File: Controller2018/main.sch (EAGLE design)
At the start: 110 parts, among them Q1 MOSFET-NCHANNELDFN5X6, Q2 MOSFET-NCHANNELDFN5X6, Q3 MOSFET-NCHANNELDFN5X6, Q4 MOSFET-NCHANNELDFN5X6, Q5 MOSFET-NCHANNELDFN5X6, Q6 MOSFET-NCHANNELDFN5X6, Q7 MOSFET-PCHANNEL, U1 TEENSY_3.0+4, U2 DRV8301

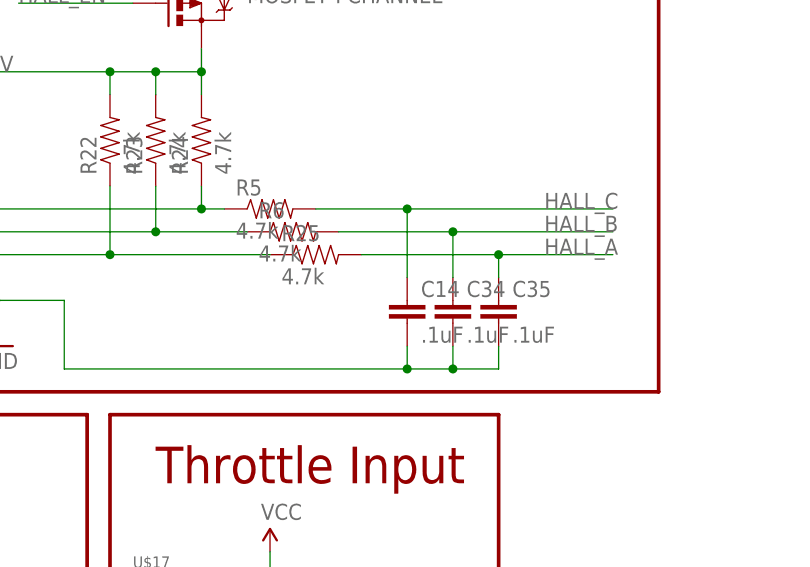
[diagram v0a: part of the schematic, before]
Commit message: Updated controller values to be more realistic
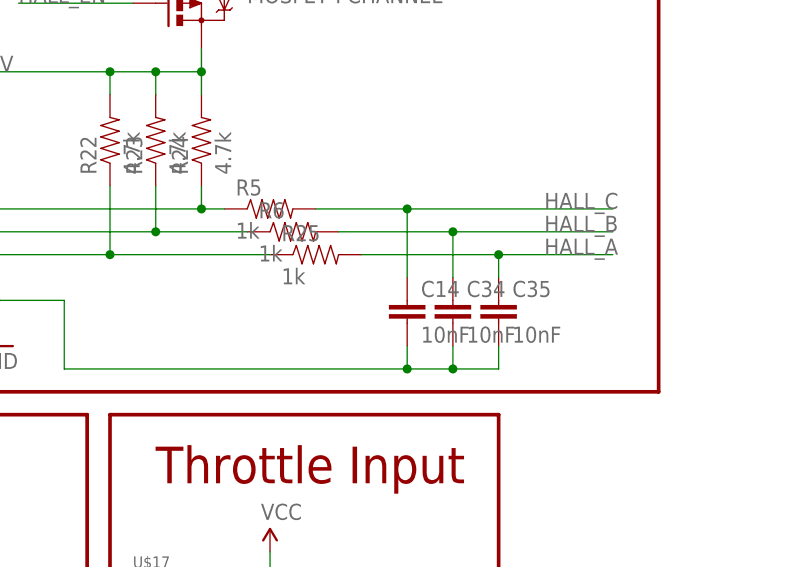
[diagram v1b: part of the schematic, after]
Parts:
- C14, C34, C35: value .1uF -> 10nF
- R25, R5, R6: value 4.7k -> 1k
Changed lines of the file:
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@@
 <?xml version="1.0" encoding="utf-8"?>
 <!DOCTYPE eagle SYSTEM "eagle.dtd">
-<eagle version="8.4.0">
+<eagle version="9.0.1">
 <drawing>
 <settings>
@@
 <part name="C28" library="SparkFun-Capacitors" deviceset="CAP" device="1206" value="4.7uF"/>
 <part name="D2" library="SparkFun-DiscreteSemi" deviceset="DIODE" device="ES3J" value="TVS"/>
-<part name="R5" library="SparkFun-Passives" deviceset="RESISTOR" device="0603-RES" value="4.7k"/>
-<part name="R6" library="SparkFun-Passives" deviceset="RESISTOR" device="0603-RES" value="4.7k"/>
-<part name="R25" library="SparkFun-Passives" deviceset="RESISTOR" device="0603-RES" value="4.7k"/>
+<part name="R5" library="SparkFun-Passives" deviceset="RESISTOR" device="0603-RES" value="1k"/>
+<part name="R6" library="SparkFun-Passives" deviceset="RESISTOR" device="0603-RES" value="1k"/>
+<part name="R25" library="SparkFun-Passives" deviceset="RESISTOR" device="0603-RES" value="1k"/>
 <part name="C39" library="SparkFun-Passives" deviceset="CAP" device="0603-CAP" value="1uF"/>
 <part name="R26" library="SparkFun-Passives" deviceset="RESISTOR" device="0603-RES" value="100k"/>
@@
 <part name="Q7" library="SparkFun-DiscreteSemi" deviceset="MOSFET-PCHANNEL" device=""/>
 <part name="U$29" library="F-J" deviceset="VCC" device=""/>
-<part name="C14" library="SparkFun-Passives" deviceset="CAP" device="0603-CAP" value=".1uF"/>
-<part name="C34" library="SparkFun-Passives" deviceset="CAP" device="0603-CAP" value=".1uF"/>
-<part name="C35" library="SparkFun-Passives" deviceset="CAP" device="0603-CAP" value=".1uF"/>
+<part name="C14" library="SparkFun-Passives" deviceset="CAP" device="0603-CAP" value="10nF"/>
+<part name="C34" library="SparkFun-Passives" deviceset="CAP" device="0603-CAP" value="10nF"/>
+<part name="C35" library="SparkFun-Passives" deviceset="CAP" device="0603-CAP" value="10nF"/>
 <part name="U$12" library="2018" deviceset="OPAMP_QUAD" device=""/>
 <part name="R31" library="SparkFun-Resistors" deviceset="RESISTOR" device="0603" value="16.2k"/>
